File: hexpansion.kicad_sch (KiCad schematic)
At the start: 44 parts, among them J1 Hexpansion-Connector, J2 Conn_ARM_SWD_TagConnect_TC2030, Q1 2N7002, Q2 2N7002, Q3 2N7002, Q4 2N7002

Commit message: fixes, some footprints
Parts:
- JP2, JP3, JP4: footprint (none) -> Jumper:SolderJumper-2_P1.3mm_Open_RoundedPad1.0x1.5mm
- TP1, TP10, TP2, TP3, TP4, TP5, TP6, TP7, TP8, TP9: footprint (none) -> TestPoint:TestPoint_Pad_2.0x2.0mm
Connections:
- net HS_I: no longer names the net of J1.19 (HS_I)
- net LS_A: no longer names the net of J1.2 (LS_A)
- net LS_B: no longer names the net of J1.3 (LS_B)
- net LS_C: no longer names the net of J1.7 (LS_C)
- net LS_D: no longer names the net of J1.8 (LS_D)
- net LS_E: no longer names the net of J1.9 (LS_E)
- no-connect marks 1 -> 7
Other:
- note added: "TTL output? needed to pull up, at least on previous board"
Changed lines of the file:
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@@
 	)
 	(no_connect
+		(at 48.26 35.56)
+	)
+	(no_connect
+		(at 48.26 50.8)
+	)
+	(no_connect
+		(at 48.26 38.1)
+	)
+	(no_connect
+		(at 48.26 30.48)
+	)
+	(no_connect
 		(at 73.66 144.78)
 	)
+	(no_connect
+		(at 48.26 33.02)
+	)
+	(no_connect
+		(at 48.26 27.94)
+	)
 	(wire
 		(pts
@@
 		)
 	)
+	(text "TTL output?\nneeded to pull up, at least on previous board"
+		(exclude_from_sim no)
+		(at 234.95 41.148 0)
+		(effects
+			(font
+				(size 1.27 1.27)
+			)
+			(justify left)
+		)
+	)
 	(text "Vf = 1 V - 1.5 V\nAssume typ Vf = 1.25 V\ntarget If = 20 mA\nR = (3.3 V - 1.25 V) / 20 mA\n  = 102.5 Ohm ~= 100 Ohm\nIf = 18 mA - 23 mA"
 		(exclude_from_sim no)
@@
 		)
 	)
-	(label "LS_E"
-		(at 48.26 38.1 0)
-		(fields_autoplaced yes)
-		(effects
-			(font
-				(size 1.27 1.27)
-			)
-			(justify left bottom)
-		)
-	)
-	(label "LS_A"
-		(at 48.26 27.94 0)
-		(fields_autoplaced yes)
-		(effects
-			(font
-				(size 1.27 1.27)
-			)
-			(justify left bottom)
-		)
-	)
 	(label "GND"
 		(at 38.1 78.74 0)
@@
 		)
 	)
-	(label "HS_I"
-		(at 48.26 50.8 0)
-		(fields_autoplaced yes)
-		(effects
-			(font
-				(size 1.27 1.27)
-			)
-			(justify left bottom)
-		)
-	)
 	(label "IR_TX"
 		(at 228.6 127 0)
@@
 		)
 	)
-	(label "LS_C"
-		(at 48.26 33.02 0)
-		(fields_autoplaced yes)
-		(effects
-			(font
-				(size 1.27 1.27)
-			)
-			(justify left bottom)
-		)
-	)
 	(label "HS_G"
 		(at 48.26 45.72 0)
@@
 		)
 	)
-	(label "LS_D"
-		(at 48.26 35.56 0)
-		(fields_autoplaced yes)
-		(effects
-			(font
-				(size 1.27 1.27)
-			)
-			(justify left bottom)
-		)
-	)
 	(label "HEXP_DET"
 		(at 22.86 53.34 180)
@@
 		)
 	)
-	(label "LS_B"
-		(at 48.26 30.48 0)
-		(fields_autoplaced yes)
-		(effects
-			(font
-				(size 1.27 1.27)
-			)
-			(justify left bottom)
-		)
-	)
 	(label "IR_TX"
 		(at 177.8 127 0)
@@
 			)
 		)
-		(property "Footprint" ""
+		(property "Footprint" "TestPoint:TestPoint_Pad_2.0x2.0mm"
 			(at 134.62 91.44 0)
 			(effects
@@
 		(fields_autoplaced yes)
 		(property "Reference" "TP1"
-			(at 27.94 173.2279 0)
+			(at 27.94 174.4979 0)
 			(effects
 				(font
@@
 				)
 				(justify left)
+				(hide yes)
 			)
 		)
-		(property "Footprint" ""
+		(property "Footprint" "TestPoint:TestPoint_Pad_2.0x2.0mm"
 			(at 30.48 177.8 0)
 			(effects
@@
 		(fields_autoplaced yes)
 		(property "Reference" "TP2"
-			(at 27.94 185.9279 0)
+			(at 27.94 187.1979 0)
 			(effects
 				(font
@@
 				)
 				(justify left)
+				(hide yes)
 			)
 		)
-		(property "Footprint" ""
+		(property "Footprint" "TestPoint:TestPoint_Pad_2.0x2.0mm"
 			(at 30.48 190.5 0)
 			(effects
@@
 			)
 		)
-		(property "Footprint" ""
+		(property "Footprint" "TestPoint:TestPoint_Pad_2.0x2.0mm"
 			(at 134.62 106.68 0)
 			(effects
@@
 			)
 		)
-		(property "Footprint" ""
+		(property "Footprint" "Jumper:SolderJumper-2_P1.3mm_Open_RoundedPad1.0x1.5mm"
 			(at 67.31 43.18 0)
 			(effects
@@
 			)
 		)
-		(property "Footprint" ""
+		(property "Footprint" "Jumper:SolderJumper-2_P1.3mm_Open_RoundedPad1.0x1.5mm"
 			(at 67.31 48.26 0)
 			(effects
@@
 			)
 		)
-		(property "Footprint" ""
+		(property "Footprint" "TestPoint:TestPoint_Pad_2.0x2.0mm"
 			(at 134.62 96.52 0)
 			(effects
@@
 			)
 		)
-		(property "Footprint" ""
+		(property "Footprint" "TestPoint:TestPoint_Pad_2.0x2.0mm"
 			(at 134.62 109.22 0)
 			(effects
@@
 			)
 		)
-		(property "Footprint" ""
+		(property "Footprint" "TestPoint:TestPoint_Pad_2.0x2.0mm"
 			(at 134.62 73.66 0)
 			(effects
@@
 			)
 		)
-		(property "Footprint" ""
+		(property "Footprint" "TestPoint:TestPoint_Pad_2.0x2.0mm"
 			(at 134.62 86.36 0)
 			(effects
@@
 		(fields_autoplaced yes)
 		(property "Reference" "JP1"
-			(at 34.29 72.39 0)
+			(at 34.29 74.93 0)
 			(effects
 				(font
@@
 					(size 1.27 1.27)
 				)
+				(hide yes)
 			)
 		)
@@
 			)
 		)
-		(property "Footprint" ""
+		(property "Footprint" "TestPoint:TestPoint_Pad_2.0x2.0mm"
 			(at 134.62 83.82 0)
 			(effects
@@
 			)
 		)
-		(property "Footprint" ""
+		(property "Footprint" "Jumper:SolderJumper-2_P1.3mm_Open_RoundedPad1.0x1.5mm"
 			(at 67.31 45.72 0)
 			(effects
@@
 			)
 		)
-		(property "Footprint" ""
+		(property "Footprint" "TestPoint:TestPoint_Pad_2.0x2.0mm"
 			(at 134.62 81.28 0)
 			(effects

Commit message: assign footprints
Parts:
- C1, C2: footprint (none) -> Capacitor_SMD:C_0805_2012Metric
- C3: footprint (none) -> Capacitor_SMD:C_0402_1005Metric
- D1, D2, D3, D4: footprint (none) -> LED_SMD:LED_0805_2012Metric
- R1, R10, R12, R13, R2, R4, R6, R7, R8: footprint (none) -> Resistor_SMD:R_0402_1005Metric
- R11, R3, R5, R9: footprint (none) -> Resistor_SMD:R_0805_2012Metric
- U2: footprint (none) -> parts:IRM-H6XXT
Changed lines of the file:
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@@
 			)
 		)
-		(property "Footprint" ""
+		(property "Footprint" "Resistor_SMD:R_0402_1005Metric"
 			(at 76.2 68.58 0)
 			(effects
@@
 			)
 		)
-		(property "Footprint" ""
+		(property "Footprint" "Resistor_SMD:R_0402_1005Metric"
 			(at 200.66 127 0)
 			(effects
@@
 			)
 		)
-		(property "Footprint" ""
+		(property "Footprint" "LED_SMD:LED_0805_2012Metric"
 			(at 261.62 118.11 0)
 			(effects
@@
 			)
 		)
-		(property "Footprint" ""
+		(property "Footprint" "LED_SMD:LED_0805_2012Metric"
 			(at 210.82 118.11 0)
 			(effects
@@
 			)
 		)
-		(property "Footprint" ""
+		(property "Footprint" "Capacitor_SMD:C_0805_2012Metric"
 			(at 228.6 34.29 0)
 			(effects
@@
 			)
 		)
-		(property "Footprint" ""
+		(property "Footprint" "Resistor_SMD:R_0402_1005Metric"
 			(at 251.46 127 0)
 			(effects
@@
 			)
 		)
-		(property "Footprint" ""
+		(property "Footprint" "Resistor_SMD:R_0805_2012Metric"
 			(at 210.82 73.66 0)
 			(effects
@@
 			)
 		)
-		(property "Footprint" ""
+		(property "Footprint" "Resistor_SMD:R_0402_1005Metric"
 			(at 210.82 111.76 0)
 			(effects
@@
 			)
 		)
-		(property "Footprint" ""
+		(property "Footprint" "Capacitor_SMD:C_0402_1005Metric"
 			(at 127 139.7 0)
 			(effects
@@
 			)
 		)
-		(property "Footprint" ""
+		(property "Footprint" "LED_SMD:LED_0805_2012Metric"
 			(at 210.82 80.01 0)
 			(effects
@@
 			)
 		)
-		(property "Footprint" ""
+		(property "Footprint" "Resistor_SMD:R_0402_1005Metric"
 			(at 160.02 76.2 0)
 			(effects
@@
 			)
 		)
-		(property "Footprint" ""
+		(property "Footprint" "Resistor_SMD:R_0402_1005Metric"
 			(at 152.4 73.66 0)
 			(effects
@@
 			)
 		)
-		(property "Footprint" ""
+		(property "Footprint" "LED_SMD:LED_0805_2012Metric"
 			(at 261.62 80.01 0)
 			(effects
@@
 			)
 		)
-		(property "Footprint" ""
+		(property "Footprint" "Resistor_SMD:R_0805_2012Metric"
 			(at 233.68 29.21 0)
 			(effects
@@
 			)
 		)
-		(property "Footprint" ""
+		(property "Footprint" "Resistor_SMD:R_0805_2012Metric"
 			(at 261.62 111.76 0)
 			(effects
@@
 			)
 		)
-		(property "Footprint" ""
+		(property "Footprint" "Resistor_SMD:R_0402_1005Metric"
 			(at 200.66 88.9 0)
 			(effects
@@
 			)
 		)
-		(property "Footprint" ""
+		(property "Footprint" "Resistor_SMD:R_0805_2012Metric"
 			(at 261.62 73.66 0)
 			(effects
@@
 			)
 		)
-		(property "Footprint" ""
+		(property "Footprint" "Resistor_SMD:R_0402_1005Metric"
 			(at 245.11 34.29 0)
 			(effects
@@
 			)
 		)
-		(property "Footprint" ""
+		(property "Footprint" "Capacitor_SMD:C_0805_2012Metric"
 			(at 114.3 139.7 0)
 			(effects
@@
 			)
 		)
-		(property "Footprint" ""
+		(property "Footprint" "Resistor_SMD:R_0402_1005Metric"
 			(at 251.46 88.9 0)
 			(effects
@@
 			)
 		)
-		(property "Footprint" ""
+		(property "Footprint" "parts:IRM-H6XXT"
 			(at 215.9 38.1 0)
 			(effects

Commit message: rough place of pcb
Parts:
- R7: footprint Resistor_SMD:R_0402_1005Metric -> Resistor_SMD:R_0805_2012Metric
- TP10, TP3, TP4, TP5, TP6, TP7, TP8, TP9: footprint TestPoint:TestPoint_Pad_2.0x2.0mm -> TestPoint:TestPoint_Pad_1.0x1.0mm
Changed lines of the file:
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@@
 			)
 		)
-		(property "Footprint" "TestPoint:TestPoint_Pad_2.0x2.0mm"
+		(property "Footprint" "TestPoint:TestPoint_Pad_1.0x1.0mm"
 			(at 134.62 91.44 0)
 			(effects
@@
 			)
 		)
-		(property "Footprint" "Resistor_SMD:R_0402_1005Metric"
+		(property "Footprint" "Resistor_SMD:R_0805_2012Metric"
 			(at 210.82 111.76 0)
 			(effects
@@
 			)
 		)
-		(property "Footprint" "TestPoint:TestPoint_Pad_2.0x2.0mm"
+		(property "Footprint" "TestPoint:TestPoint_Pad_1.0x1.0mm"
 			(at 134.62 106.68 0)
 			(effects
@@
 			)
 		)
-		(property "Footprint" "TestPoint:TestPoint_Pad_2.0x2.0mm"
+		(property "Footprint" "TestPoint:TestPoint_Pad_1.0x1.0mm"
 			(at 134.62 96.52 0)
 			(effects
@@
 			)
 		)
-		(property "Footprint" "TestPoint:TestPoint_Pad_2.0x2.0mm"
+		(property "Footprint" "TestPoint:TestPoint_Pad_1.0x1.0mm"
 			(at 134.62 109.22 0)
 			(effects
@@
 			)
 		)
-		(property "Footprint" "TestPoint:TestPoint_Pad_2.0x2.0mm"
+		(property "Footprint" "TestPoint:TestPoint_Pad_1.0x1.0mm"
 			(at 134.62 73.66 0)
 			(effects
@@
 			)
 		)
-		(property "Footprint" "TestPoint:TestPoint_Pad_2.0x2.0mm"
+		(property "Footprint" "TestPoint:TestPoint_Pad_1.0x1.0mm"
 			(at 134.62 86.36 0)
 			(effects
@@
 			)
 		)
-		(property "Footprint" "TestPoint:TestPoint_Pad_2.0x2.0mm"
+		(property "Footprint" "TestPoint:TestPoint_Pad_1.0x1.0mm"
 			(at 134.62 83.82 0)
 			(effects
@@
 			)
 		)
-		(property "Footprint" "TestPoint:TestPoint_Pad_2.0x2.0mm"
+		(property "Footprint" "TestPoint:TestPoint_Pad_1.0x1.0mm"
 			(at 134.62 81.28 0)
 			(effects

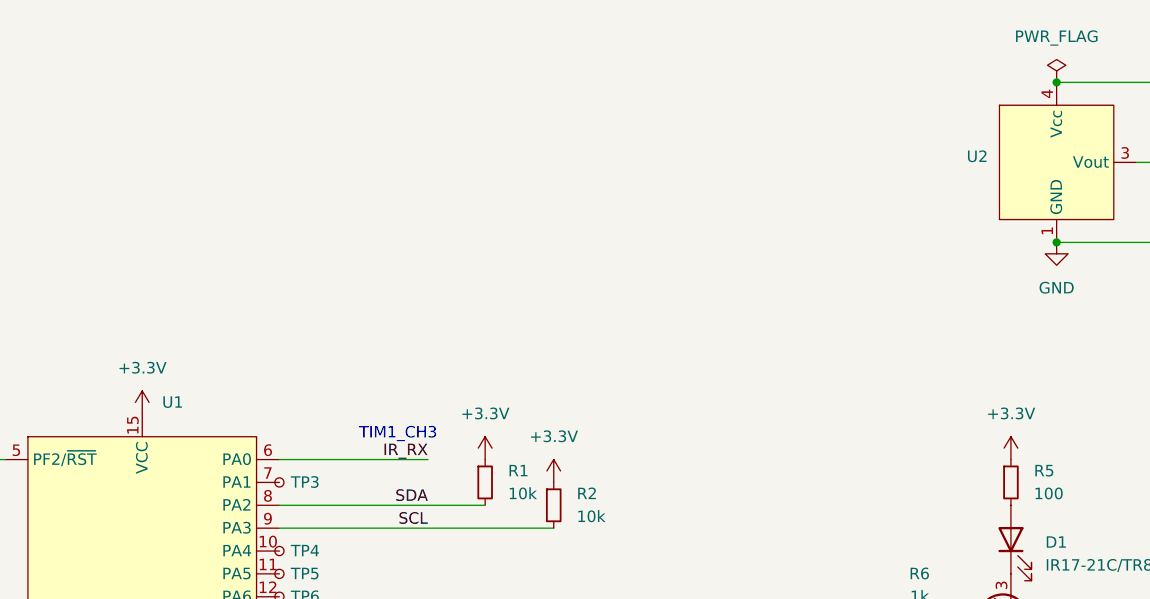
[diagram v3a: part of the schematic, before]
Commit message: clean up silk/fab
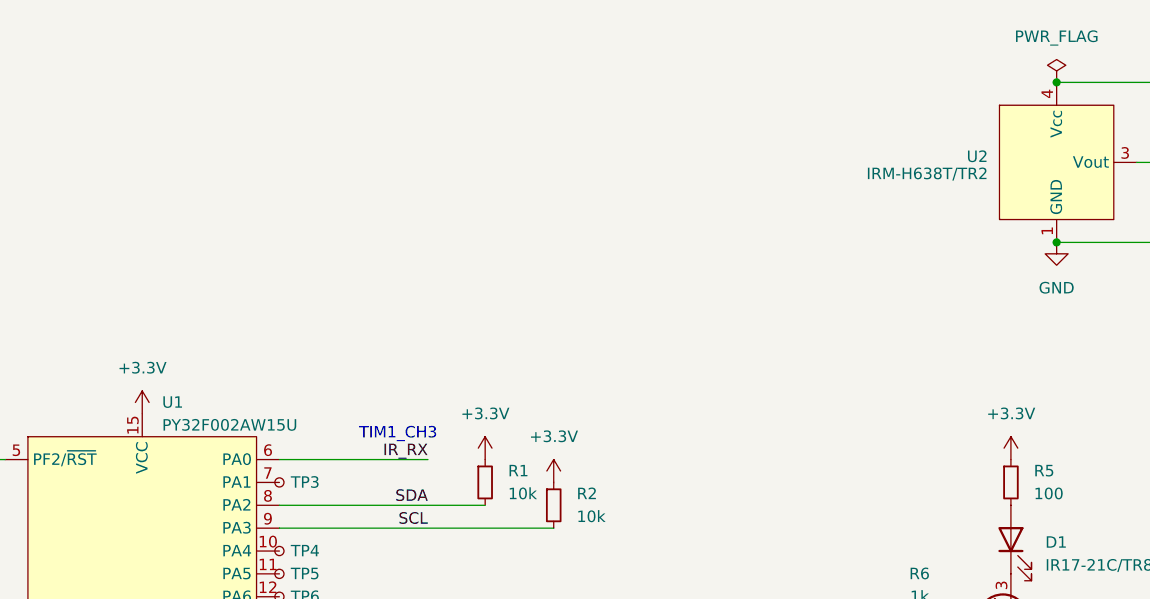
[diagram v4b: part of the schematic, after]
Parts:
- JP2: value SolderJumper_2_Open -> SWCLK
- JP3: value SolderJumper_2_Open -> SWDIO
- JP4: value SolderJumper_2_Open -> ~{RST}
- TP1: value TestPoint -> SCL
- TP10: value TestPoint_Small -> PB1
- TP2: value TestPoint -> SDA
- TP3: value TestPoint_Small -> PA1
- TP4: value TestPoint_Small -> PA4
- TP5: value TestPoint_Small -> PA5
- TP6: value TestPoint_Small -> PA6
- TP7: value TestPoint_Small -> PA8
- TP8: value TestPoint_Small -> PA12
- TP9: value TestPoint_Small -> PB0
- U1: value ~ -> PY32F002AW15U
- U2: value ~ -> IRM-H638T/TR2
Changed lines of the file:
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@@
 			)
 		)
-		(property "Value" "TestPoint_Small"
+		(property "Value" "PA8"
 			(at 130.81 92.7099 0)
 			(effects
@@
 			)
 		)
-		(property "Value" "~"
+		(property "Value" "PY32F002AW15U"
 			(at 116.4941 67.31 0)
 			(effects
@@
 			)
 		)
-		(property "Value" "TestPoint"
+		(property "Value" "SCL"
 			(at 27.94 175.7679 0)
 			(effects
@@
 			)
 		)
-		(property "Value" "TestPoint"
+		(property "Value" "SDA"
 			(at 27.94 188.4679 0)
 			(effects
@@
 			)
 		)
-		(property "Value" "TestPoint_Small"
+		(property "Value" "PB0"
 			(at 130.81 107.9499 0)
 			(effects
@@
 			)
 		)
+		(property "Sim.Enable" "0"
+			(at 0 81.28 0)
+			(effects
+				(font
+					(size 1.27 1.27)
+				)
+				(hide yes)
+			)
+		)
+		(property "exclude_from_bom" ""
+			(at 0 81.28 0)
+			(effects
+				(font
+					(size 1.27 1.27)
+				)
+				(hide yes)
+			)
+		)
 		(pin "8"
 		)
@@
 			)
 		)
-		(property "Value" "SolderJumper_2_Open"
+		(property "Value" "SWCLK"
 			(at 67.31 39.37 0)
 			(effects
@@
 			)
 		)
-		(property "Value" "SolderJumper_2_Open"
+		(property "Value" "~{RST}"
 			(at 67.31 44.45 0)
 			(effects
@@
 			)
 		)
-		(property "Value" "TestPoint_Small"
+		(property "Value" "PA12"
 			(at 130.81 97.7899 0)
 			(effects
@@
 			)
 		)
-		(property "Value" "TestPoint_Small"
+		(property "Value" "PB1"
 			(at 130.81 110.4899 0)
 			(effects
@@
 			)
 		)
-		(property "Value" "TestPoint_Small"
+		(property "Value" "PA1"
 			(at 130.81 74.9299 0)
 			(effects
@@
 			)
 		)
-		(property "Value" "TestPoint_Small"
+		(property "Value" "PA6"
 			(at 130.81 87.6299 0)
 			(effects
@@
 			)
 		)
-		(property "Value" "TestPoint_Small"
+		(property "Value" "PA5"
 			(at 130.81 85.0899 0)
 			(effects
@@
 			)
 		)
-		(property "Value" "SolderJumper_2_Open"
+		(property "Value" "SWDIO"
 			(at 67.31 41.91 0)
 			(effects
@@
 			)
 		)
-		(property "Value" "~"
+		(property "Value" "IRM-H638T/TR2"
 			(at 208.28 39.37 0)
 			(effects
@@
 			)
 		)
-		(property "Value" "TestPoint_Small"
+		(property "Value" "PA4"
 			(at 130.81 82.5499 0)
 			(effects

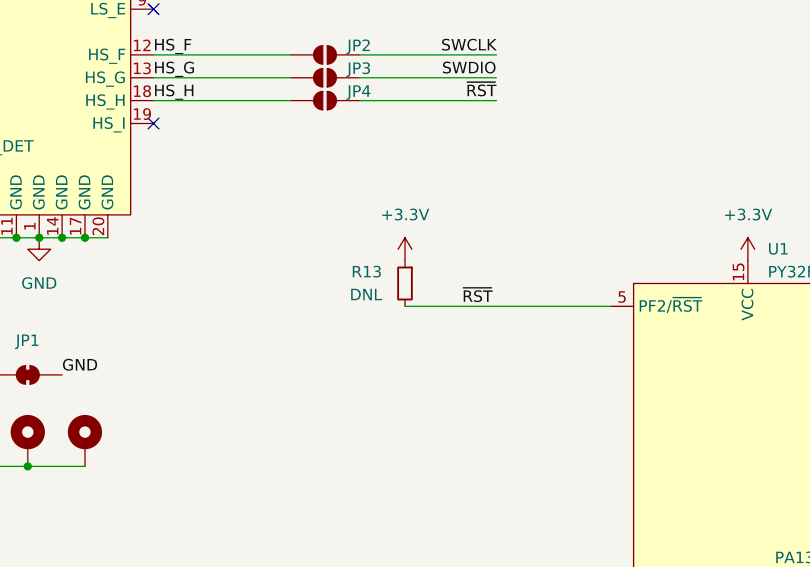
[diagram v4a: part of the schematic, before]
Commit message: add LCSC part numbers
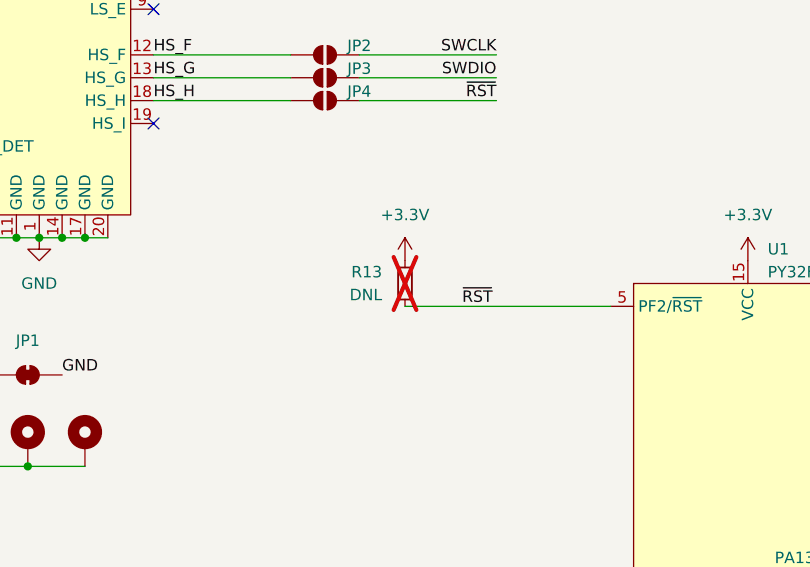
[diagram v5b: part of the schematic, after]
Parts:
- C1, C2: LCSC (none) -> C1779
- C3: LCSC (none) -> C1525
- D1, D2, D3, D4: LCSC (none) -> C131250
- Q1, Q2, Q3, Q4: LCSC (none) -> C7420321
- R1, R2, R4: LCSC (none) -> C25744
- R10, R12, R6, R8: LCSC (none) -> C11702
- R11, R3, R5, R7, R9: LCSC (none) -> C17408
- R13: now not fitted
- U1: LCSC (none) -> C5291740
- U2: LCSC (none) -> C91447
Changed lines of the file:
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@@
 			)
 		)
+		(property "LCSC" "C7420321"
+			(at 208.28 127 0)
+			(effects
+				(font
+					(size 1.27 1.27)
+				)
+				(hide yes)
+			)
+		)
 		(pin "1"
 		)
@@
 		(in_bom yes)
 		(on_board yes)
-		(dnp no)
+		(dnp yes)
 		(property "Reference" "R13"
 			(at 73.66 67.3099 0)
@@
 			)
 		)
+		(property "LCSC" "C5291740"
+			(at 114.3 88.9 0)
+			(effects
+				(font
+					(size 1.27 1.27)
+				)
+				(hide yes)
+			)
+		)
 		(pin "1"
 		)
@@
 			)
 		)
+		(property "LCSC" "C7420321"
+			(at 259.08 88.9 0)
+			(effects
+				(font
+					(size 1.27 1.27)
+				)
+				(hide yes)
+			)
+		)
 		(pin "1"
 		)
@@
 			)
 		)
+		(property "LCSC" "C11702"
+			(at 200.66 127 0)
+			(effects
+				(font
+					(size 1.27 1.27)
+				)
+				(hide yes)
+			)
+		)
 		(pin "2"
 		)
@@
 			)
 		)
+		(property "LCSC" "C131250"
+			(at 261.62 118.11 0)
+			(effects
+				(font
+					(size 1.27 1.27)
+				)
+				(hide yes)
+			)
+		)
 		(pin "1"
 		)
@@
 			)
 		)
+		(property "LCSC" "C131250"
+			(at 210.82 118.11 0)
+			(effects
+				(font
+					(size 1.27 1.27)
+				)
+				(hide yes)
+			)
+		)
 		(pin "1"
 		)
@@
 			)
 		)
+		(property "LCSC" "C7420321"
+			(at 259.08 127 0)
+			(effects
+				(font
+					(size 1.27 1.27)
+				)
+				(hide yes)
+			)
+		)
 		(pin "1"
 		)
@@
 			)
 		)
+		(property "LCSC" "C1779"
+			(at 228.6 34.29 0)
+			(effects
+				(font
+					(size 1.27 1.27)
+				)
+				(hide yes)
+			)
+		)
 		(pin "1"
 		)
@@
 			)
 		)
+		(property "LCSC" "C11702"
+			(at 251.46 127 0)
+			(effects
+				(font
+					(size 1.27 1.27)
+				)
+				(hide yes)
+			)
+		)
 		(pin "2"
 		)
@@
 			)
 		)
+		(property "LCSC" "C17408"
+			(at 210.82 73.66 0)
+			(effects
+				(font
+					(size 1.27 1.27)
+				)
+				(hide yes)
+			)
+		)
 		(pin "2"
 		)
@@
 			)
 		)
+		(property "LCSC" "C17408"
+			(at 210.82 111.76 0)
+			(effects
+				(font
+					(size 1.27 1.27)
+				)
+				(hide yes)
+			)
+		)
 		(pin "2"
 		)
@@
 			)
 		)
+		(property "LCSC" "C1525"
+			(at 127 139.7 0)
+			(effects
+				(font
+					(size 1.27 1.27)
+				)
+				(hide yes)
+			)
+		)
 		(pin "2"
 		)
@@
 			)
 		)
+		(property "LCSC" "C131250"
+			(at 210.82 80.01 0)
+			(effects
+				(font
+					(size 1.27 1.27)
+				)
+				(hide yes)
+			)
+		)
 		(pin "1"
 		)
@@
 			)
 		)
+		(property "LCSC" "C25744"
+			(at 160.02 76.2 0)
+			(effects
+				(font
+					(size 1.27 1.27)
+				)
+				(hide yes)
+			)
+		)
 		(pin "1"
 		)
@@
 			)
 		)
+		(property "LCSC" "C25744"
+			(at 152.4 73.66 0)
+			(effects
+				(font
+					(size 1.27 1.27)
+				)
+				(hide yes)
+			)
+		)
 		(pin "1"
 		)
@@
 		(at 35.56 40.64 0)
 		(unit 1)
-		(exclude_from_sim no)
+		(exclude_from_sim yes)
 		(in_bom no)
 		(on_board yes)
@@
 			)
 		)
-		(property "Sim.Enable" "0"
-			(at 0 81.28 0)
-			(effects
-				(font
-					(size 1.27 1.27)
-				)
-				(hide yes)
-			)
-		)
 		(property "exclude_from_bom" ""
 			(at 0 81.28 0)
@@
 			)
 		)
+		(property "LCSC" "C131250"
+			(at 261.62 80.01 0)
+			(effects
+				(font
+					(size 1.27 1.27)
+				)
+				(hide yes)
+			)
+		)
 		(pin "1"
 		)
@@
 			)
 		)
+		(property "LCSC" "C17408"
+			(at 233.68 29.21 0)
+			(effects
+				(font
+					(size 1.27 1.27)
+				)
+				(hide yes)
+			)
+		)
 		(pin "2"
 		)
@@
 			)
 		)
+		(property "LCSC" "C17408"
+			(at 261.62 111.76 0)
+			(effects
+				(font
+					(size 1.27 1.27)
+				)
+				(hide yes)
+			)
+		)
 		(pin "2"
 		)
@@
 			)
 		)
+		(property "LCSC" "C11702"
+			(at 200.66 88.9 0)
+			(effects
+				(font
+					(size 1.27 1.27)
+				)
+				(hide yes)
+			)
+		)
 		(pin "2"
 		)
@@
 			)
 		)
+		(property "LCSC" "C17408"
+			(at 261.62 73.66 0)
+			(effects
+				(font
+					(size 1.27 1.27)
+				)
+				(hide yes)
+			)
+		)
 		(pin "2"
 		)
@@
 			)
 		)
+		(property "LCSC" "C25744"
+			(at 245.11 34.29 0)
+			(effects
+				(font
+					(size 1.27 1.27)
+				)
+				(hide yes)
+			)
+		)
 		(pin "1"
 		)
@@
 			)
 		)
+		(property "LCSC" "C7420321"
+			(at 208.28 88.9 0)
+			(effects
+				(font
+					(size 1.27 1.27)
+				)
+				(hide yes)
+			)
+		)
 		(pin "1"
 		)
@@
 			)
 		)
+		(property "LCSC" "C1779"
+			(at 114.3 139.7 0)
+			(effects
+				(font
+					(size 1.27 1.27)
+				)
+				(hide yes)
+			)
+		)
 		(pin "2"
 		)
@@
 			)
 		)
+		(property "LCSC" "C11702"
+			(at 251.46 88.9 0)
+			(effects
+				(font
+					(size 1.27 1.27)
+				)
+				(hide yes)
+			)
+		)
 		(pin "2"
 		)
@@
 			(at 215.9 38.1 0)
 			(effects
+				(font
+					(size 1.27 1.27)
+				)
+				(hide yes)
+			)
+		)
+		(property "LCSC" "C91447"
+			(at 215.9 38.1 0)
+			(effects
